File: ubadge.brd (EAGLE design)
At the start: 10 x 10 mm, 9 parts, among them IC1 ATTINY85

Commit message: fixed mislabled DM/DP (no board change)
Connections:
- net DM-TINY: now also IC1.2, R1.2; no longer IC1.3, R2.2
- net DP-TINY: now also IC1.3, R2.2; no longer IC1.2, R1.2
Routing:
- net DP-TINY: track 6.48 -> 5.47 mm
- net DM-TINY: track 5.47 -> 6.48 mm
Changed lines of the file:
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@@
 <wire x1="4.334" y1="9.1138" x2="2.4638" y2="9.3726" width="0.254" layer="1"/>
 </signal>
-<signal name="DP-TINY">
+<signal name="DM-TINY">
 <contactref element="R1" pad="2"/>
 <contactref element="IC1" pad="2"/>
@@
 <wire x1="6.8142" y1="3.28090625" x2="6.8142" y2="4.2345875" width="0.1524" layer="1"/>
 </signal>
-<signal name="DM-TINY">
+<signal name="DP-TINY">
 <contactref element="R2" pad="2"/>
 <contactref element="IC1" pad="3"/>

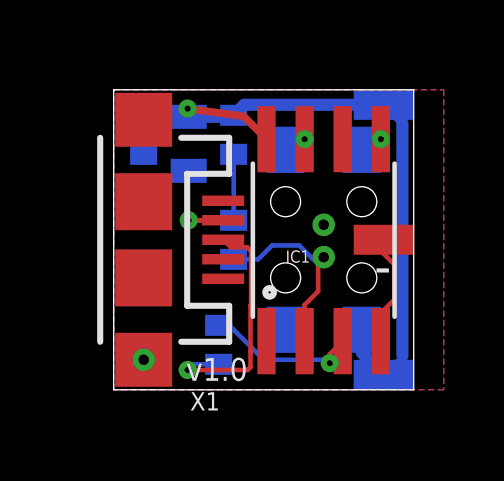
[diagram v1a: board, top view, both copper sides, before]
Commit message: swapped in usb connector with throughole alignment tabs and adjusted a few components. adding centroid, cam, and gerbv files.
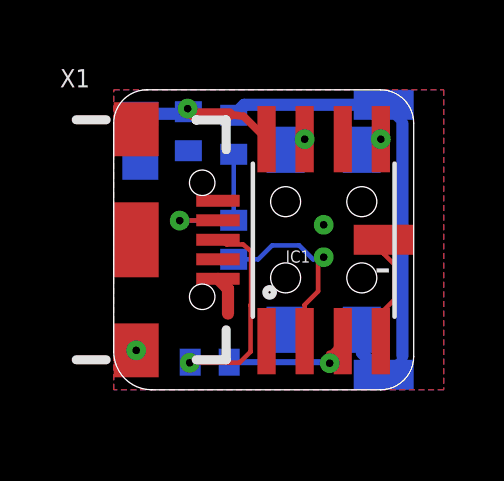
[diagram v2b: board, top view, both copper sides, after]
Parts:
- X1: device SparkFun-Connectors:USB-MICROB -> SparkFun-Connectors:USB-B-MICRO-SMD
- moved C2 1.61 mm to (0.89, 8.30)
- moved C1 1.49 mm to (2.49, 8.62)
- moved R2 0.65 mm to (3.20, 0.92), turned to 180 degrees
- moved X1 0.25 mm to (0.75, 5.00), turned to 0 degrees
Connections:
- net GND: now also X1.SHIELD1, X1.SHIELD2, X1.SHIELD3; no longer X1.MT1, X1.MT2, X1.P$1, X1.P$2
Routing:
- net DP: track 8.21 -> 6.79 mm
- net GND: track 3.85 -> 5.15 mm
- net VCC: track 24.8 -> 23.7 mm
- net DP-TINY: track 5.47 -> 4.61 mm
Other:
- outline, holes or cut-outs redrawn
- board text added: "v1.1"
- board text removed: "v1.0"
